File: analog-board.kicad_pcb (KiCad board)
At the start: 2 copper layers, 200 x 150 mm, 481 parts, among them J1 AC IN, J2 OUT, J3 CONN_20X2, P2 CONN_01X02, Q1 2N3906, Q10 2N3906, Q11 2N3906, Q12 2N3906, Q13 2N3906, Q14 2N3906, Q15 2N3906, Q16 2N3906, Q17 NPN, Q18 NPN, Q19 J111, Q2 2N3906, Q20 2N3906, Q3 2N3906, Q4 2N3906, Q5 2N3906, Q6 BCM857BS, Q7 2N3906, Q8 2N3906, Q9 2N3906, U1 LM13700, U10 ADR01, U11 DG212B, U12 DG212B, U13 DG408, U14 DG408, U15 TL072-, U16 DG408, U17 DG408, U18 LM13700, U19 LM13700, U2 LM13700, U21 TL072-, U22 TL074-, U23 TL074-, U24 TL074-, U25 TL074-, U26 TL072-, U27 TL074-, U28 TL074-, U29 LM13700, U3 LM13700, U30 LM13700, U31 TL074-, U32 LM13700, U33 TL074-, U34 TL074-, U35 TL074-, U36 74LV573, U38 0 - 10V, U39 TL074-, U4 DG212B, U40 DG419, U41 0 - 10V, U42 10 - 0V, U43 LM7812, U44 LM7912, U45 DG408, U46 7805, U5 TL074-, U6 AD5556, U7 TL072-, U8 TL074-, U9 AD8672

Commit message: routing S&H CV traces. Need to move U14 over to the left to shorten 7 out of 8 CV traces
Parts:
- C114, C115: moved to F.Cu
- moved C114 4.03 mm to (27.0, 8.00), turned to 180 degrees
- moved C30 3.81 mm to (33.0, 58.0)
- moved C115 3.54 mm to (40.5, 8.00), turned to 0 degrees
- moved C36 3.20 mm to (103.0, 58.0)
- moved C42 2.92 mm to (118.0, 58.0)
- moved C44 2.92 mm to (140.0, 58.0), turned to 90 degrees
- moved TP28 2.69 mm to (25.5, 4.00)
- moved C34 2.50 mm to (80.5, 58.0)
- moved C32 2.12 mm to (65.5, 58.0)
- moved C46 2.12 mm to (155.0, 58.0)
- moved C45 2.06 mm to (155.0, 51.0)
- moved C28 1.80 mm to (18.0, 58.0)
- moved C27 1.58 mm to (18.0, 51.0)
- moved C29 1.58 mm to (33.0, 51.0)
- moved C31 1.58 mm to (65.5, 51.0)
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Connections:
- C49 pad 1: SH3 -> SH2
- C50 pad 1: SH2 -> SH3
- C51 pad 1: SH0 -> SH1
- C52 pad 1: SH1 -> SH0
- C53 pad 1: SH7 -> SH6
- C54 pad 1: SH6 -> SH7
- U22 pad 10: SH0 -> SH1
- U22 pad 12: SH1 -> SH0
- U22 pad 3: SH3 -> SH2
- U22 pad 5: SH2 -> SH3
- U23 pad 3: SH7 -> SH6
- U23 pad 5: SH6 -> SH7
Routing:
- net -12V: track 736.5 -> 957.9 mm, vias 14 -> 18
- net OSCB PITCH CV: track 0.00 -> 143.3 mm
- net +12V: track 1231.1 -> 1350.9 mm, vias 12 -> 16
- net GLIDE AMT CV: track 0.00 -> 118.5 mm
- net OSCA PITCH CV: track 0.00 -> 108.2 mm
- net OSC EG2 AMT CV: track 0.00 -> 99.2 mm
- net PWM B CV: track 0.00 -> 98.6 mm, vias 0 -> 2
- net OSCB INIT CV: track 0.00 -> 95.1 mm, vias 0 -> 2
- net OSCA MIX CV: track 0.00 -> 73.6 mm
- net OSCB MIX CV: track 0.00 -> 44.7 mm
- net DB2: track 128.9 -> 172.4 mm, vias 0 -> 2
- net DB1: track 128.6 -> 168.5 mm, vias 0 -> 2
- net DB0: track 142.1 -> 178.3 mm, vias 0 -> 2
- net SH0: track 2.49 -> 22.5 mm
- net SH6: track 2.49 -> 21.1 mm
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
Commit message: routing routing routing
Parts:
- moved C24 10.5 mm to (57.5, 42.0)
- moved C26 10.5 mm to (67.5, 42.0)
- moved C31 10.5 mm to (55.0, 51.0)
- moved C32 10.5 mm to (55.0, 58.0)
- moved C33 10.5 mm to (70.0, 51.0)
- moved C34 10.5 mm to (70.0, 58.0)
- moved C57 10.5 mm to (61.0, 55.0)
- moved C58 10.5 mm to (61.0, 53.0)
- moved C59 10.5 mm to (49.0, 53.0)
- moved C60 10.5 mm to (49.0, 55.0)
- moved C61 10.5 mm to (76.0, 55.0)
- moved C62 10.5 mm to (76.0, 53.0)
- moved C63 10.5 mm to (64.0, 55.0)
- moved C64 10.5 mm to (64.0, 53.0)
- moved U14 10.5 mm to (62.5, 44.5)
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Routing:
- net EG2: track 13.1 -> 262.2 mm, vias 0 -> 5
- net +5V: track 111.9 -> 349.5 mm, vias 4 -> 8
- net OSCB SAW WAVE: track 67.3 -> 178.0 mm, vias 3 -> 5
- net Net-(C14-Pad2): track 4.54 -> 78.5 mm, vias 0 -> 1
- net OSCB MIX CV: track 44.7 -> 0.65 mm
- net +12V: track 1350.9 -> 1393.1 mm, vias 16 -> 20
- net OSCB MOD: track 0.00 -> 33.4 mm, vias 0 -> 1
- net -12V: track 957.9 -> 990.9 mm, vias 18 -> 20
- net Net-(R58-Pad2): track 1.51 -> 25.2 mm
- net Net-(C12-Pad2): track 4.58 -> 27.7 mm, vias 0 -> 1
- net Net-(R60-Pad2): track 0.00 -> 21.5 mm, vias 0 -> 1
- net VDAC: track 194.2 -> 173.5 mm
- net Net-(C16-Pad2): track 4.07 -> 21.9 mm
- net Net-(R57-Pad1): track 0.00 -> 17.5 mm
- net Net-(R139-Pad2): track 0.00 -> 16.8 mm
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
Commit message: routing
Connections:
- C69 pad 1: SH20 -> SH22
- C70 pad 1: SH21 -> SH23
- C71 pad 1: SH22 -> SH21
- C72 pad 1: SH23 -> SH20
- U28 pad 10: SH22 -> SH21
- U28 pad 12: SH23 -> SH20
- U28 pad 3: SH20 -> SH22
- U28 pad 5: SH21 -> SH23
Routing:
- net GATE: track 0.00 -> 158.0 mm
- net FIL EG2 AMT CV: track 0.00 -> 120.5 mm
- net VOL CV: track 0.00 -> 110.4 mm
- net AMP LFO AMT CV: track 0.00 -> 96.4 mm
- net KEYTRACK AMT CV: track 0.00 -> 95.2 mm
- net FIL OSCB  AMT CV: track 0.00 -> 87.4 mm
- net FIL LFO AMT CV: track 0.00 -> 64.2 mm
- net OSCB MIX CV: track 0.65 -> 58.4 mm
- net +12V: track 1393.1 -> 1443.6 mm, vias 20 -> 23
- net RES CV: track 0.00 -> 43.4 mm, vias 0 -> 1
- net CUTOFF CV: track 0.00 -> 42.6 mm
- net -12V: track 990.9 -> 1032.1 mm
- net OSC EG2 MOD: track 37.3 -> 76.4 mm, vias 1 -> 2
- net Net-(R200-Pad2): track 0.00 -> 33.7 mm
- net Net-(C86-Pad2): track 0.00 -> 26.3 mm
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
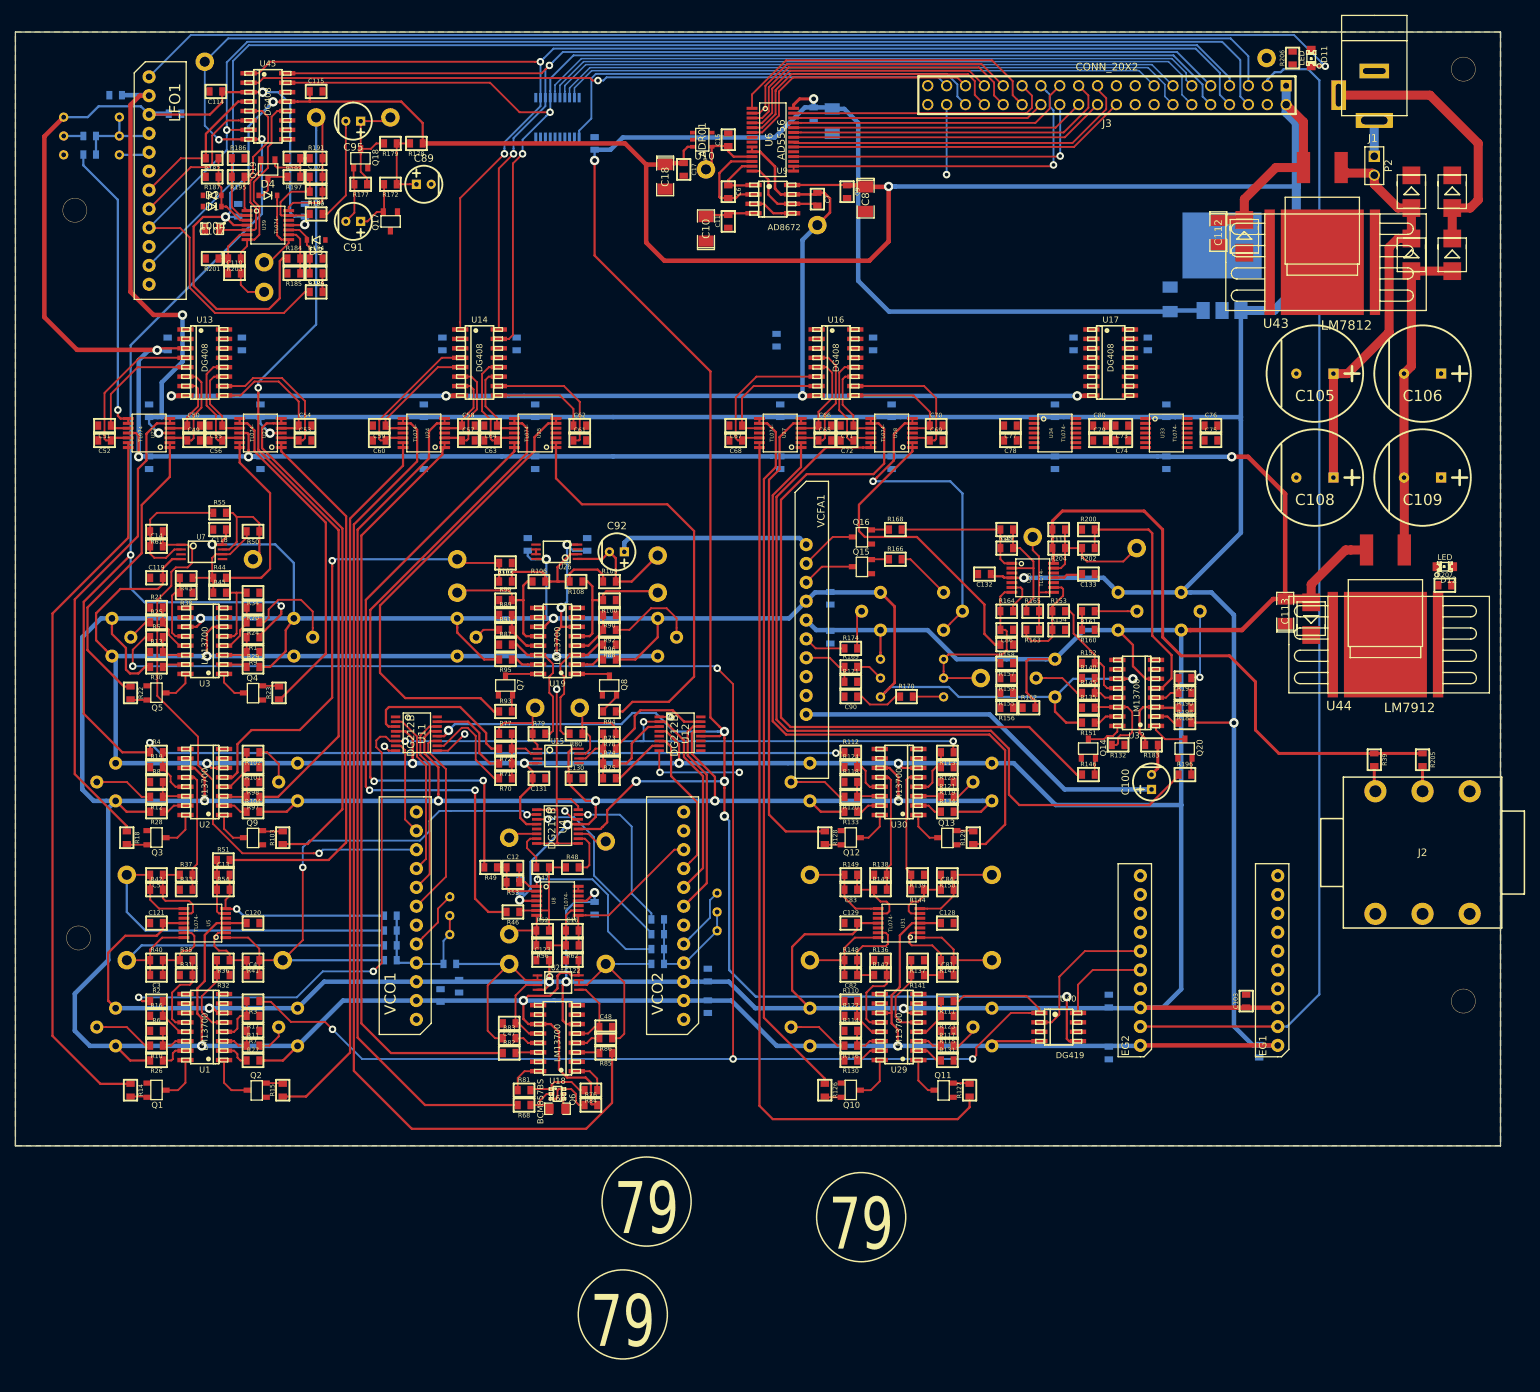
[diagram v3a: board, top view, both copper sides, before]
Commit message: all CVs routed, just need to adjust EG1 and EG2 CVs
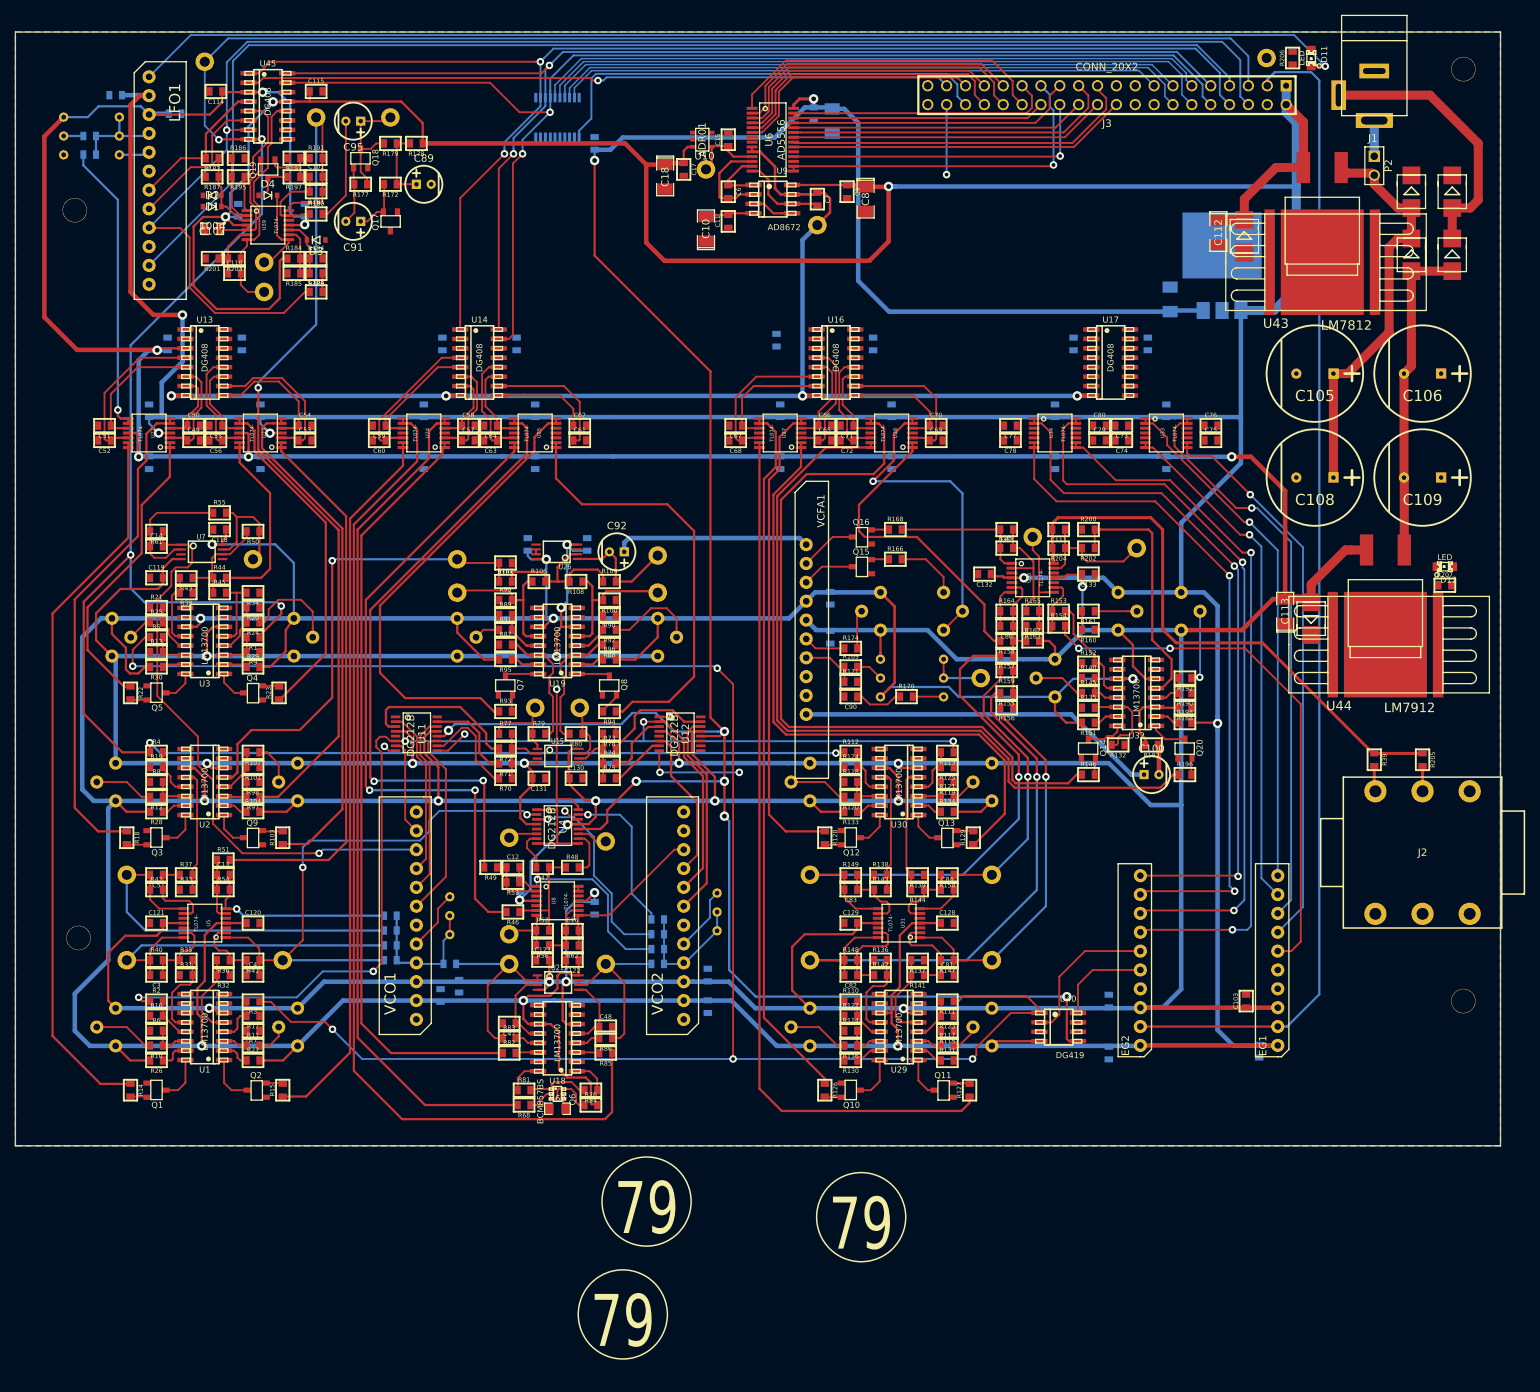
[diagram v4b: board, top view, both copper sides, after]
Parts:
- moved R162 9.01 mm to (137.0, 82.0)
- moved C100 1.00 mm to (153.0, 100.0), turned to 0 degrees
- moved R157 1.00 mm to (133.5, 84.0)
- moved R159 1.00 mm to (133.5, 86.0)
- moved C86 0.50 mm to (133.5, 80.0)
- moved R154 0.50 mm to (140.5, 80.0)
- moved R158 0.50 mm to (133.5, 82.0)
- moved R163 0.50 mm to (137.0, 80.0)
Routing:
- net EG2 REL CV: track 0.00 -> 98.7 mm, vias 0 -> 2
- net EG2 SUS CV: track 0.00 -> 95.7 mm, vias 0 -> 2
- net EG2 ATT CV: track 0.00 -> 94.5 mm, vias 0 -> 2
- net EG2 DEC CV: track 0.00 -> 92.3 mm, vias 0 -> 2
- net EG1 REL CV: track 0.00 -> 76.8 mm, vias 0 -> 1
- net EG1 SUS CV: track 0.00 -> 75.5 mm, vias 0 -> 1
- net EG1: track 0.00 -> 72.4 mm, vias 0 -> 2
- net EG1 ATT CV: track 0.00 -> 69.9 mm, vias 0 -> 1
- net EG1 DEC CV: track 0.00 -> 69.5 mm, vias 0 -> 1
- net Net-(C82-Pad2): track 13.4 -> 77.9 mm, vias 0 -> 1
- net Net-(C83-Pad2): track 12.9 -> 73.8 mm, vias 0 -> 1
- net Net-(C81-Pad2): track 13.8 -> 53.4 mm, vias 0 -> 1
- net Net-(C84-Pad2): track 13.2 -> 46.3 mm, vias 0 -> 1
- net Net-(C86-Pad1): track 5.00 -> 19.8 mm
- net Net-(C86-Pad2): track 26.3 -> 13.3 mm
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
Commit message: flippled main 40 pin connector to work with connector on digital board - reconnected all traces
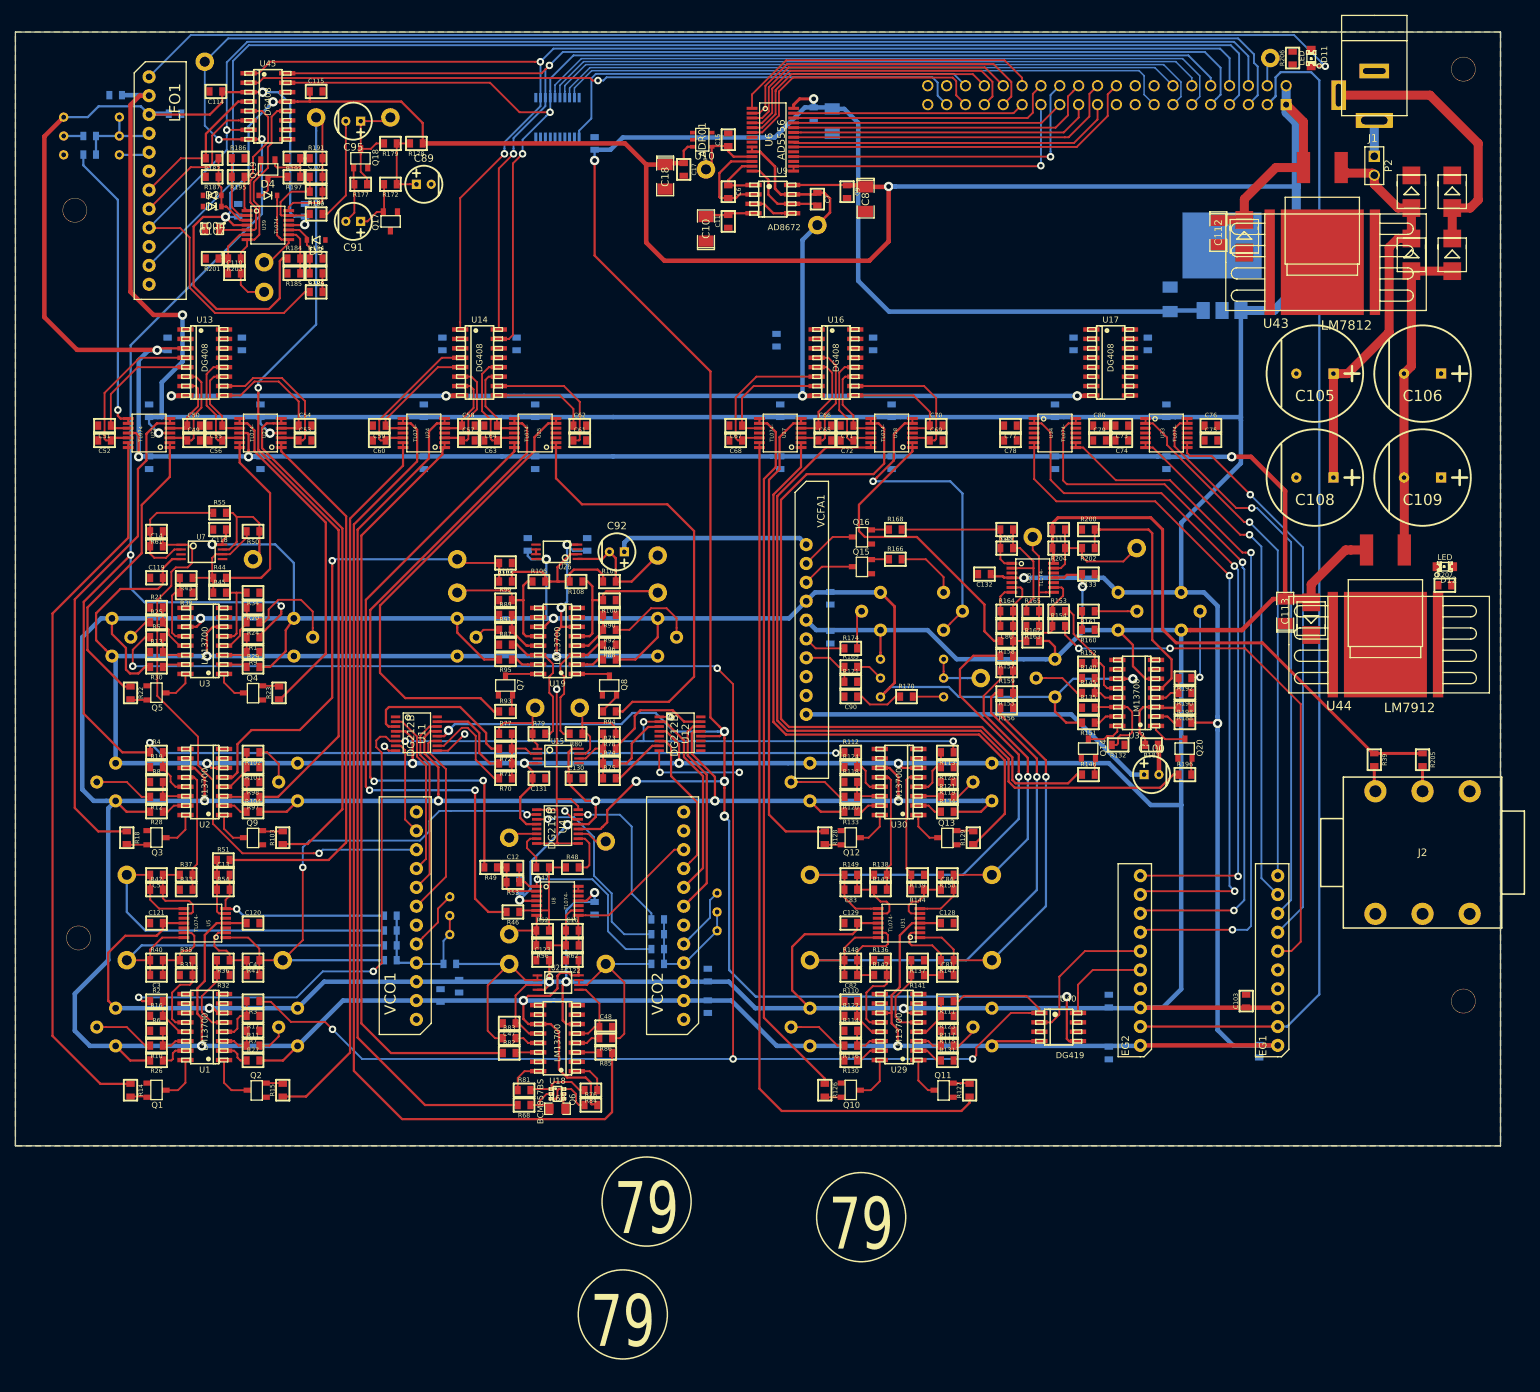
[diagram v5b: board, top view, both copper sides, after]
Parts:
- J3: moved to B.Cu
- moved TP24 0.50 mm to (169.0, 3.50)
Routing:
- net EG2 POL: track 9.43 -> 0.00 mm, vias 1 -> 0
- net LFO RESET: track 170.2 -> 176.5 mm
- net DB1: track 165.8 -> 171.7 mm
- net ~DAC WR: track 47.1 -> 42.2 mm
- net /DAC6: track 35.9 -> 31.2 mm
- net /DAC4: track 39.5 -> 43.9 mm
- net /DAC2: track 36.9 -> 41.3 mm
- net DB5: track 85.9 -> 90.2 mm
- net DB3: track 91.0 -> 95.3 mm
- net LFO: track 389.1 -> 393.3 mm
- net TUNE: track 48.9 -> 52.8 mm
- net /DAC10: track 44.6 -> 41.0 mm
- net /DAC12: track 47.7 -> 44.3 mm
- net /DAC11: track 42.8 -> 46.1 mm
- net /DAC13: track 45.8 -> 48.6 mm
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
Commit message: routing
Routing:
- net EG2 POL: track 0.00 -> 169.8 mm, vias 0 -> 3
- net SH24: track 0.00 -> 20.7 mm
- net SH25: track 0.00 -> 16.8 mm
- net SH27: track 0.00 -> 2.49 mm
- net SH26: track 0.00 -> 2.49 mm
- net EG1 SUS CV: track 75.5 -> 73.8 mm
- net EG1 REL CV: track 76.8 -> 75.2 mm
- net EG1 DEC CV: track 69.5 -> 68.2 mm
- net EG2 DEC CV: track 92.3 -> 91.6 mm
- net EG2 REL CV: track 98.7 -> 98.0 mm
- net EG2 ATT CV: track 94.5 -> 94.0 mm

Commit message: getting close to finishing routing signal and power traces
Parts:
- moved C37 13.5 mm to (116.0, 41.5)
- moved D12 3.81 mm to (194.0, 68.5), turned to 0 degrees
- moved C39 3.54 mm to (116.0, 45.5), turned to 270 degrees
- moved C40 3.54 mm to (153.0, 45.5), turned to 270 degrees
- moved R207 3.35 mm to (194.0, 71.5), turned to 180 degrees
- moved C88 1.50 mm to (79.5, 15.0)
- moved C38 0.50 mm to (142.5, 41.5)
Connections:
- C73 pad 1: SH30 -> SH31
- C74 pad 1: SH31 -> SH30
- C79 pad 1: SH27 -> SH26
- C80 pad 1: SH26 -> SH27
- U33 pad 3: SH30 -> SH31
- U33 pad 5: SH31 -> SH30
- U34 pad 10: SH27 -> SH26
- U34 pad 12: SH26 -> SH27
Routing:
- net -12V: track 1033.4 -> 1225.7 mm, vias 21 -> 33
- net DAC MUX EN0: track 0.00 -> 163.9 mm, vias 0 -> 1
- net OSC SYNC: track 1.74 -> 139.2 mm, vias 1 -> 3
- net +12V: track 1442.4 -> 1576.5 mm, vias 23 -> 34
- net OSCA PULSE: track 0.00 -> 128.9 mm, vias 0 -> 3
- net DAC MUX EN1: track 0.00 -> 126.7 mm, vias 0 -> 1
- net OSCA TRI: track 4.63 -> 128.4 mm, vias 1 -> 3
- net OSCA SAW: track 0.00 -> 121.9 mm, vias 0 -> 3
- net OSCB MOD: track 33.4 -> 139.3 mm, vias 1 -> 3
- net OSCB PULSE: track 13.8 -> 107.6 mm, vias 2 -> 3
- net OSCB SAW: track 1.41 -> 95.2 mm, vias 1 -> 3
- net OSCB TRI: track 0.00 -> 92.0 mm, vias 0 -> 3
- net DB2: track 168.3 -> 259.6 mm, vias 2 -> 3
- net DB0: track 178.3 -> 266.0 mm
- net DB1: track 171.7 -> 256.3 mm, vias 2 -> 3
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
